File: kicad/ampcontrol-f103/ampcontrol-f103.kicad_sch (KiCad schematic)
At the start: 71 parts, among them J1 SP, J10 Buttons, J11 Encoder, J12 LCD_CTRL, J13 I2C, J14 I2C, J15 I2C, J16 SPI_2.4, J17 SPI_2.8, J18 SPI_3.2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

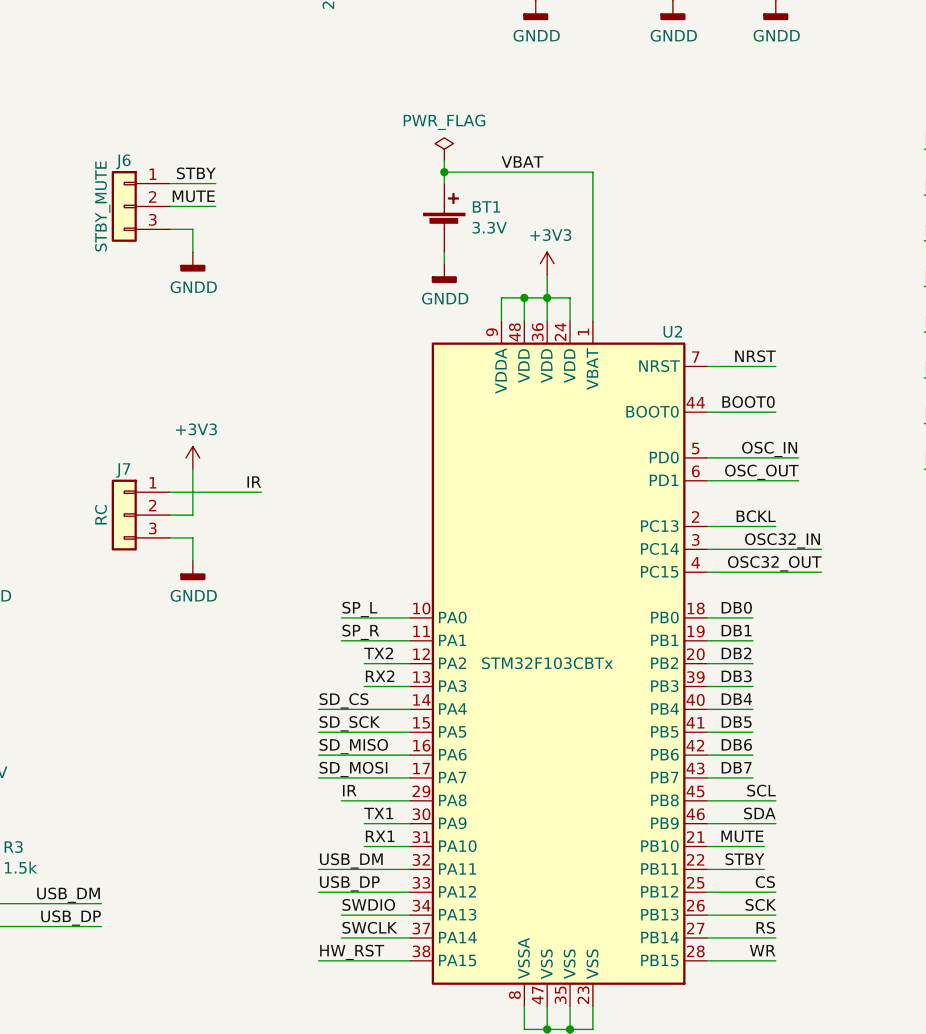
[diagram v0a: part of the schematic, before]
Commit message: Swap MUTE and STBY in schematic, with no PCB change
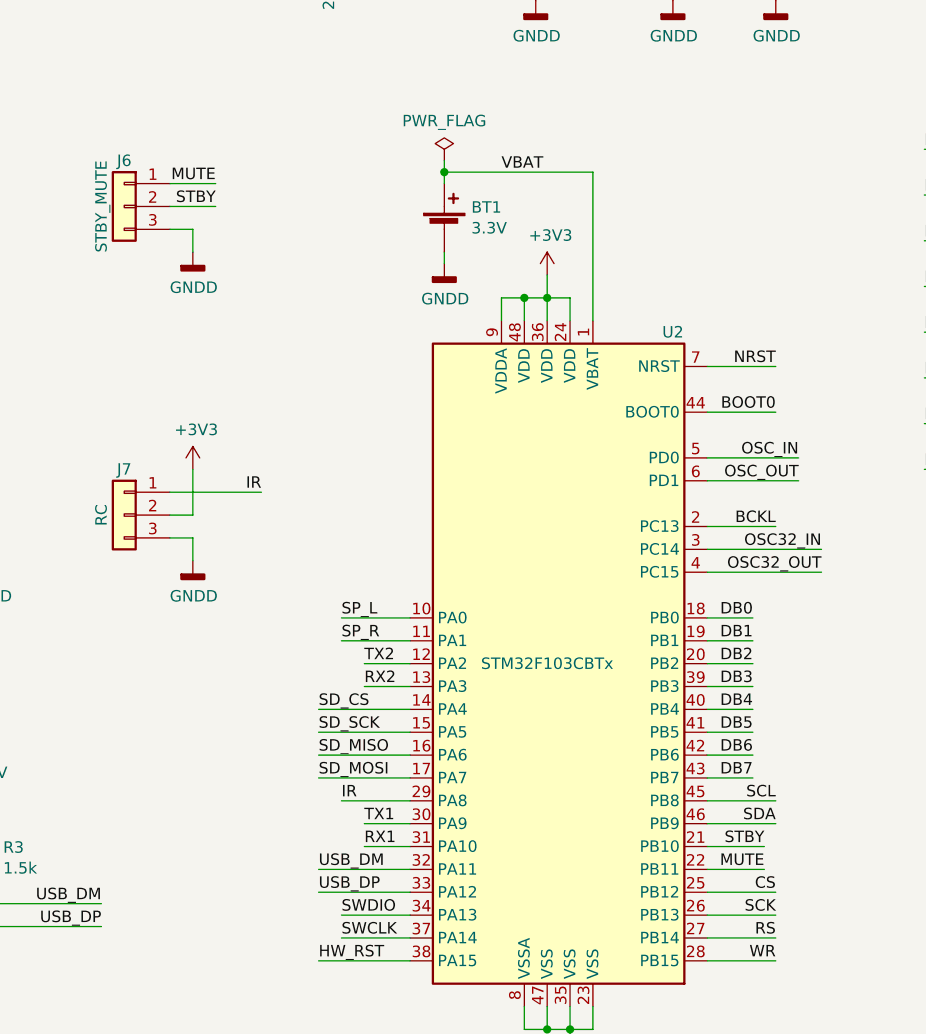
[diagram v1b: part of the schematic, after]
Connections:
- net MUTE: now also J6.1 (Pin_1), U2.22 (PB11); no longer J6.2 (Pin_2), U2.21 (PB10)
- net STBY: now also J6.2 (Pin_2), U2.21 (PB10); no longer J6.1 (Pin_1), U2.22 (PB11)
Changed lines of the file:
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@@
     (effects (font (size 1.27 1.27)) (justify right bottom))
   )
-  (label "STBY" (at 68.58 93.98 180)
+  (label "MUTE" (at 68.58 93.98 180)
     (effects (font (size 1.27 1.27)) (justify right bottom))
   )
@@
     (effects (font (size 1.27 1.27)) (justify left bottom))
   )
-  (label "MUTE" (at 68.58 96.52 180)
+  (label "STBY" (at 68.58 96.52 180)
     (effects (font (size 1.27 1.27)) (justify right bottom))
   )
@@
     (effects (font (size 1.27 1.27)) (justify right bottom))
   )
-  (label "STBY" (at 129.54 170.18 180)
+  (label "MUTE" (at 129.54 170.18 180)
     (effects (font (size 1.27 1.27)) (justify right bottom))
   )
@@
     (effects (font (size 1.27 1.27)) (justify right bottom))
   )
-  (label "MUTE" (at 129.54 167.64 180)
+  (label "STBY" (at 129.54 167.64 180)
     (effects (font (size 1.27 1.27)) (justify right bottom))
   )
@@
     (pin "2")
     (pin "3")
+    (pin "5")
+    (pin "6")
+    (pin "7")
+    (pin "4")
+    (pin "8")
   )
   (symbol (lib_id "Amplifier_Operational:MCP602") (at 78.74 60.96 0) (unit 2)
@@
       (effects (font (size 1.27 1.27)) hide)
     )
+    (pin "1")
+    (pin "2")
+    (pin "3")
     (pin "5")
     (pin "6")
     (pin "7")
+    (pin "4")
+    (pin "8")
   )
   (symbol (lib_id "Device:R") (at 220.98 132.08 0) (unit 1)
@@
       (effects (font (size 1.27 1.27)) hide)
     )
+    (pin "1")
+    (pin "2")
+    (pin "3")
+    (pin "5")
+    (pin "6")
+    (pin "7")
     (pin "4")
     (pin "8")

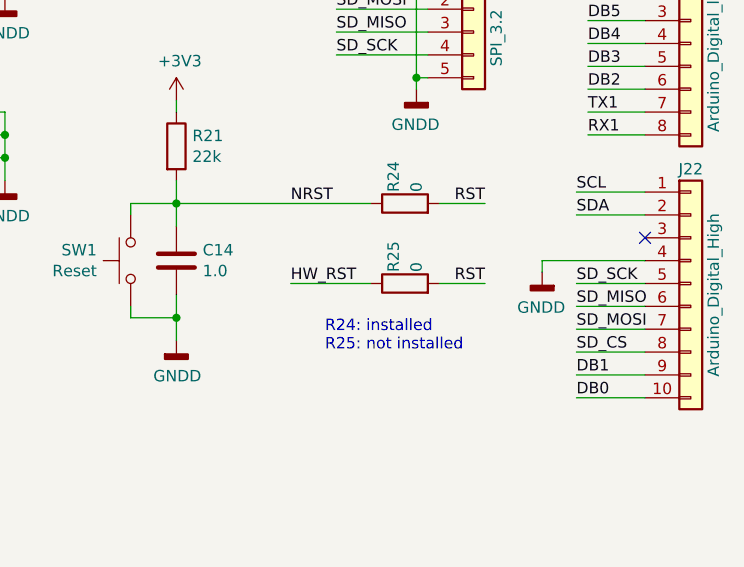
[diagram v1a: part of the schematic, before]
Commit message: kicad: sch: Mark R25 as not installed
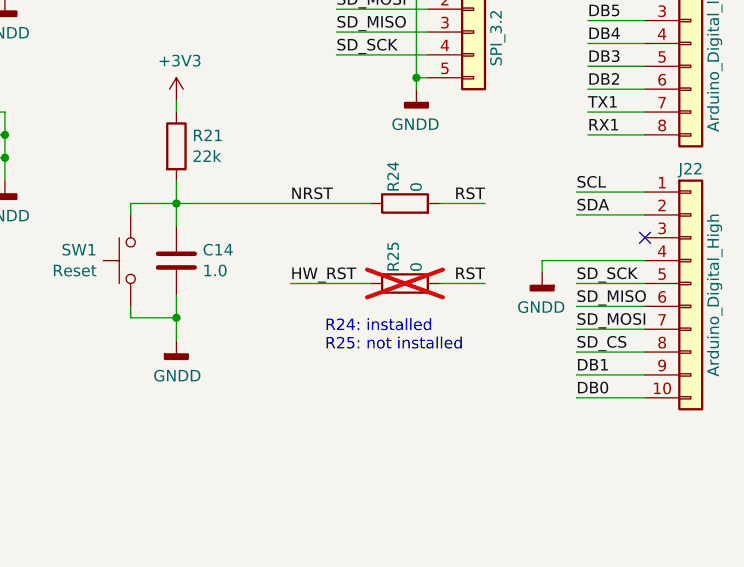
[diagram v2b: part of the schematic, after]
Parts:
- R25: now not fitted
